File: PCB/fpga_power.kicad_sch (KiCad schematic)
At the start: 11 parts, among them U1 LFE5U-25F-6BG256x

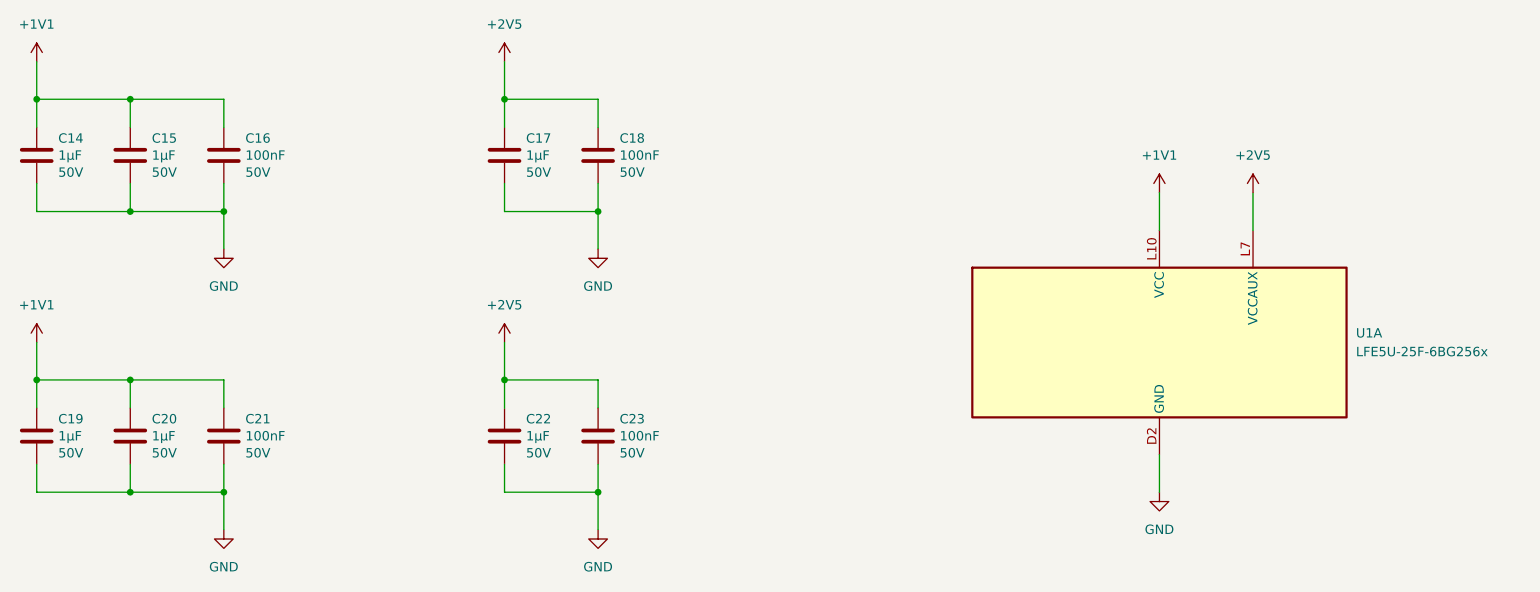
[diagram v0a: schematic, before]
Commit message: Add power supplies
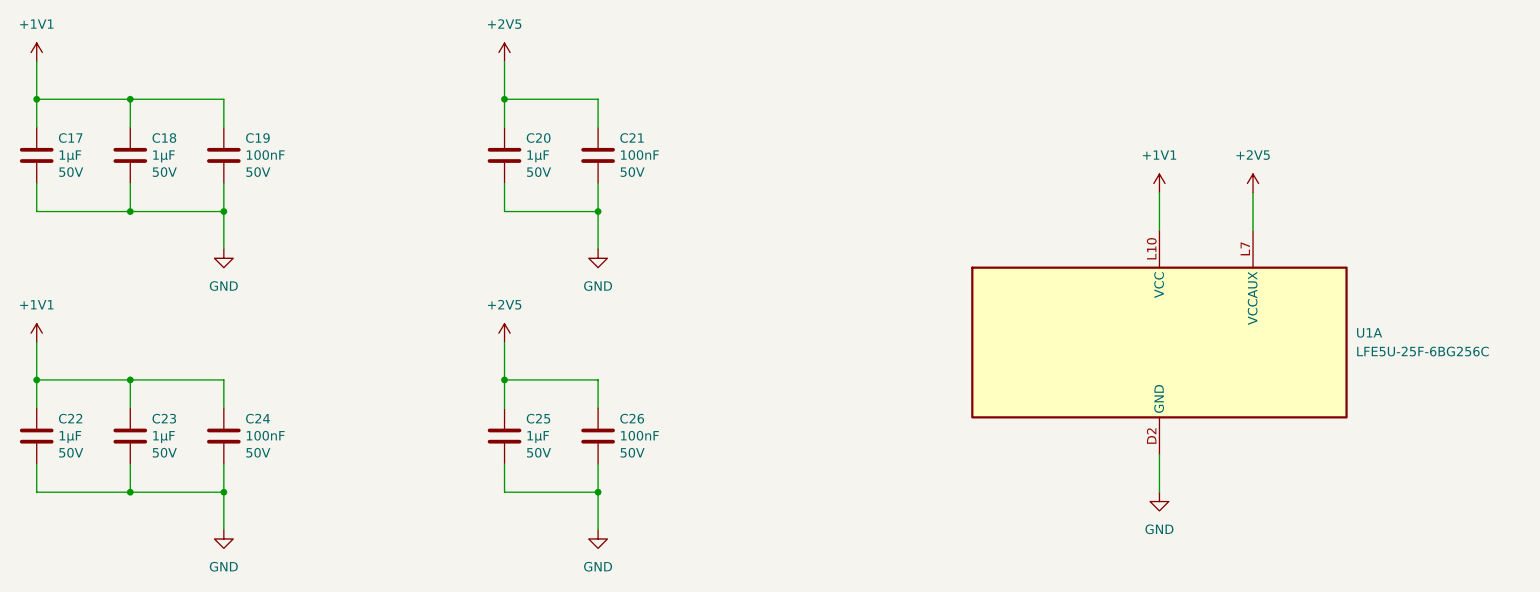
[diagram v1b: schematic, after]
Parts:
- C17: renamed from C14; footprint Capacitor_SMD:C_0603_1608Metric -> Capacitor_SMD:C_0402_1005Metric_Pad0.74x0.62mm_HandSolder; LCSC (none) -> C1518208; Part_number C1608X5R1H105K080AB -> GRM155R61H105KE05D
- C18: renamed from C15; footprint Capacitor_SMD:C_0603_1608Metric -> Capacitor_SMD:C_0402_1005Metric_Pad0.74x0.62mm_HandSolder; LCSC (none) -> C1518208; Part_number C1608X5R1H105K080AB -> GRM155R61H105KE05D
- C19: renamed from C16; footprint Capacitor_SMD:C_0603_1608Metric -> Capacitor_SMD:C_0402_1005Metric_Pad0.74x0.62mm_HandSolder; LCSC (none) -> C77020; Part_number C1608X5R1H104K080AA -> GRM155R71H104KE14D
- C20: renamed from C17; footprint Capacitor_SMD:C_0603_1608Metric -> Capacitor_SMD:C_0402_1005Metric_Pad0.74x0.62mm_HandSolder; LCSC (none) -> C1518208; Part_number C1608X5R1H105K080AB -> GRM155R61H105KE05D
- C21: renamed from C18; footprint Capacitor_SMD:C_0603_1608Metric -> Capacitor_SMD:C_0402_1005Metric_Pad0.74x0.62mm_HandSolder; LCSC (none) -> C77020; Part_number C1608X5R1H104K080AA -> GRM155R71H104KE14D
- C22: renamed from C19; footprint Capacitor_SMD:C_0603_1608Metric -> Capacitor_SMD:C_0402_1005Metric_Pad0.74x0.62mm_HandSolder; LCSC (none) -> C1518208; Part_number C1608X5R1H105K080AB -> GRM155R61H105KE05D
- C23: renamed from C20; footprint Capacitor_SMD:C_0603_1608Metric -> Capacitor_SMD:C_0402_1005Metric_Pad0.74x0.62mm_HandSolder; LCSC (none) -> C1518208; Part_number C1608X5R1H105K080AB -> GRM155R61H105KE05D
- C24: renamed from C21; footprint Capacitor_SMD:C_0603_1608Metric -> Capacitor_SMD:C_0402_1005Metric_Pad0.74x0.62mm_HandSolder; LCSC (none) -> C77020; Part_number C1608X5R1H104K080AA -> GRM155R71H104KE14D
- C25: renamed from C22; footprint Capacitor_SMD:C_0603_1608Metric -> Capacitor_SMD:C_0402_1005Metric_Pad0.74x0.62mm_HandSolder; LCSC (none) -> C1518208; Part_number C1608X5R1H105K080AB -> GRM155R61H105KE05D
- C26: renamed from C23; footprint Capacitor_SMD:C_0603_1608Metric -> Capacitor_SMD:C_0402_1005Metric_Pad0.74x0.62mm_HandSolder; LCSC (none) -> C77020; Part_number C1608X5R1H104K080AA -> GRM155R71H104KE14D
- U1: value LFE5U-25F-6BG256x -> LFE5U-25F-6BG256C; LCSC (none) -> C1521614; Part_number (none) -> LFE5U-25F-6BG256C

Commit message: Add a USB hub
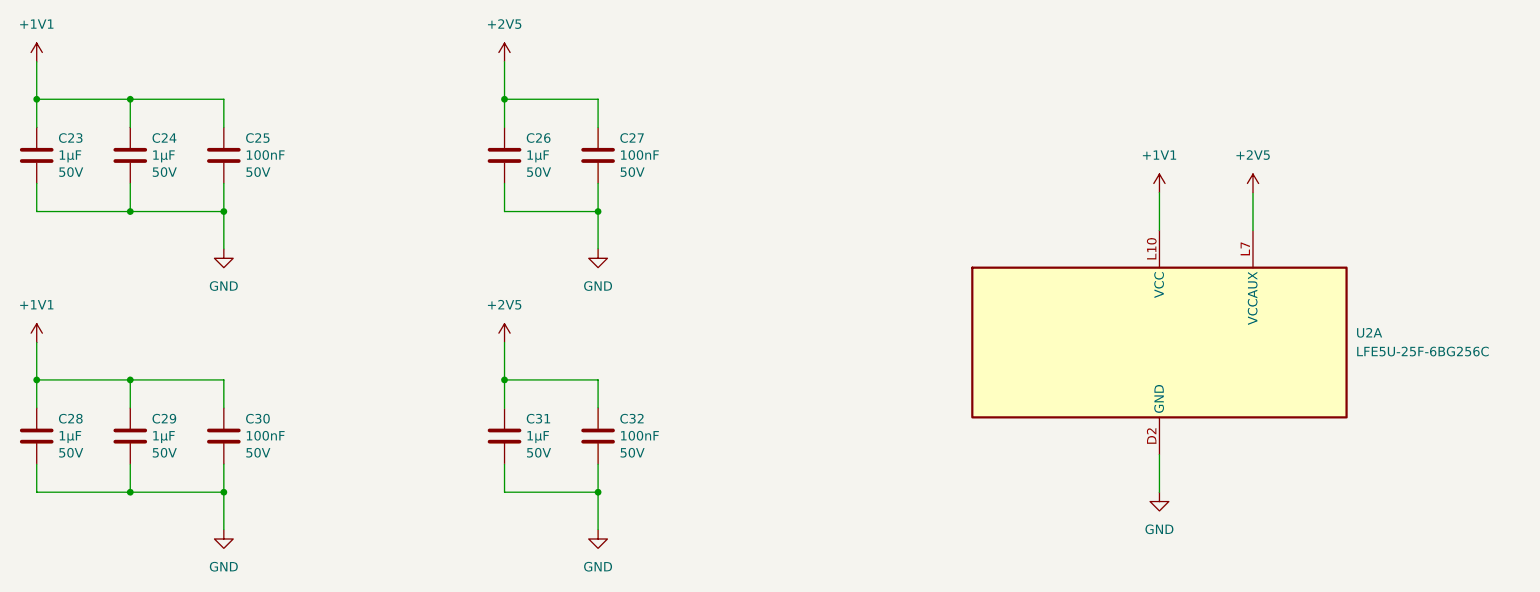
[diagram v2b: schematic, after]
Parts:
- renumbered C17 to C23, C18 to C24, C19 to C25, C20 to C26, C21 to C27, C22 to C28, C23 to C29, C24 to C30, C25 to C31, C26 to C32, U1 to U2
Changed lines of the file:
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@@
 		(on_board yes)
 		(dnp no)
-		(property "Reference" "C17"
+		(property "Reference" "C23"
 			(at 53.721 61.1886 0)
 			(effects
@@
 			(project "clavier"
 				(path "/6362c6e0-59ef-40d3-b6e0-7e9dfe7b9b20/d73938da-f0ba-48e3-aac9-a36988c25c2c/e36c52fe-7af8-49a0-bf3c-a636c30fc9cb"
-					(reference "C17")
+					(reference "C23")
 					(unit 1)
 				)
@@
 		(on_board yes)
 		(dnp no)
-		(property "Reference" "C19"
+		(property "Reference" "C25"
 			(at 79.121 61.1886 0)
 			(effects
@@
 			(project "clavier"
 				(path "/6362c6e0-59ef-40d3-b6e0-7e9dfe7b9b20/d73938da-f0ba-48e3-aac9-a36988c25c2c/e36c52fe-7af8-49a0-bf3c-a636c30fc9cb"
-					(reference "C19")
+					(reference "C25")
 					(unit 1)
 				)
@@
 		(on_board yes)
 		(dnp no)
-		(property "Reference" "C18"
+		(property "Reference" "C24"
 			(at 66.421 61.1886 0)
 			(effects
@@
 			(project "clavier"
 				(path "/6362c6e0-59ef-40d3-b6e0-7e9dfe7b9b20/d73938da-f0ba-48e3-aac9-a36988c25c2c/e36c52fe-7af8-49a0-bf3c-a636c30fc9cb"
-					(reference "C18")
+					(reference "C24")
 					(unit 1)
 				)
@@
 		(on_board yes)
 		(dnp no)
-		(property "Reference" "C23"
+		(property "Reference" "C29"
 			(at 66.421 99.2886 0)
 			(effects
@@
 			(project "clavier"
 				(path "/6362c6e0-59ef-40d3-b6e0-7e9dfe7b9b20/d73938da-f0ba-48e3-aac9-a36988c25c2c/e36c52fe-7af8-49a0-bf3c-a636c30fc9cb"
-					(reference "C23")
+					(reference "C29")
 					(unit 1)
 				)
@@
 		(on_board yes)
 		(dnp no)
-		(property "Reference" "C25"
+		(property "Reference" "C31"
 			(at 117.221 99.2886 0)
 			(effects
@@
 			(project "clavier"
 				(path "/6362c6e0-59ef-40d3-b6e0-7e9dfe7b9b20/d73938da-f0ba-48e3-aac9-a36988c25c2c/e36c52fe-7af8-49a0-bf3c-a636c30fc9cb"
-					(reference "C25")
+					(reference "C31")
 					(unit 1)
 				)
@@
 		(on_board yes)
 		(dnp no)
-		(property "Reference" "C20"
+		(property "Reference" "C26"
 			(at 117.221 61.1886 0)
 			(effects
@@
 			(project "clavier"
 				(path "/6362c6e0-59ef-40d3-b6e0-7e9dfe7b9b20/d73938da-f0ba-48e3-aac9-a36988c25c2c/e36c52fe-7af8-49a0-bf3c-a636c30fc9cb"
-					(reference "C20")
+					(reference "C26")
 					(unit 1)
 				)
@@
 		(dnp no)
 		(fields_autoplaced yes)
-		(property "Reference" "U1"
+		(property "Reference" "U2"
 			(at 229.87 87.6299 0)
 			(effects
@@
 			(project "clavier"
 				(path "/6362c6e0-59ef-40d3-b6e0-7e9dfe7b9b20/d73938da-f0ba-48e3-aac9-a36988c25c2c/e36c52fe-7af8-49a0-bf3c-a636c30fc9cb"
-					(reference "U1")
+					(reference "U2")
 					(unit 1)
 				)
@@
 		(dnp no)
 		(fields_autoplaced yes)
-		(property "Reference" "#PWR030"
+		(property "Reference" "#PWR044"
 			(at 114.3 54.61 0)
 			(effects
@@
 			(project "clavier"
 				(path "/6362c6e0-59ef-40d3-b6e0-7e9dfe7b9b20/d73938da-f0ba-48e3-aac9-a36988c25c2c/e36c52fe-7af8-49a0-bf3c-a636c30fc9cb"
-					(reference "#PWR030")
+					(reference "#PWR044")
 					(unit 1)
 				)
@@
 		(on_board yes)
 		(dnp no)
-		(property "Reference" "C26"
+		(property "Reference" "C32"
 			(at 129.921 99.2886 0)
 			(effects
@@
 			(project "clavier"
 				(path "/6362c6e0-59ef-40d3-b6e0-7e9dfe7b9b20/d73938da-f0ba-48e3-aac9-a36988c25c2c/e36c52fe-7af8-49a0-bf3c-a636c30fc9cb"
-					(reference "C26")
+					(reference "C32")
 					(unit 1)
 				)
@@
 		(dnp no)
 		(fields_autoplaced yes)
-		(property "Reference" "#PWR039"
+		(property "Reference" "#PWR053"
 			(at 127 120.65 0)
 			(effects
@@
 			(project "clavier"
 				(path "/6362c6e0-59ef-40d3-b6e0-7e9dfe7b9b20/d73938da-f0ba-48e3-aac9-a36988c25c2c/e36c52fe-7af8-49a0-bf3c-a636c30fc9cb"
-					(reference "#PWR039")
+					(reference "#PWR053")
 					(unit 1)
 				)
@@
 		(dnp no)
 		(fields_autoplaced yes)
-		(property "Reference" "#PWR032"
+		(property "Reference" "#PWR046"
 			(at 215.9 72.39 0)
 			(effects
@@
 			(project "clavier"
 				(path "/6362c6e0-59ef-40d3-b6e0-7e9dfe7b9b20/d73938da-f0ba-48e3-aac9-a36988c25c2c/e36c52fe-7af8-49a0-bf3c-a636c30fc9cb"
-					(reference "#PWR032")
+					(reference "#PWR046")
 					(unit 1)
 				)
@@
 		(dnp no)
 		(fields_autoplaced yes)
-		(property "Reference" "#PWR031"
+		(property "Reference" "#PWR045"
 			(at 203.2 72.39 0)
 			(effects
@@
 			(project "clavier"
 				(path "/6362c6e0-59ef-40d3-b6e0-7e9dfe7b9b20/d73938da-f0ba-48e3-aac9-a36988c25c2c/e36c52fe-7af8-49a0-bf3c-a636c30fc9cb"
-					(reference "#PWR031")
+					(reference "#PWR045")
 					(unit 1)
 				)
@@
 		(dnp no)
 		(fields_autoplaced yes)
-		(property "Reference" "#PWR034"
+		(property "Reference" "#PWR048"
 			(at 127 82.55 0)
 			(effects
@@
 			(project "clavier"
 				(path "/6362c6e0-59ef-40d3-b6e0-7e9dfe7b9b20/d73938da-f0ba-48e3-aac9-a36988c25c2c/e36c52fe-7af8-49a0-bf3c-a636c30fc9cb"
-					(reference "#PWR034")
+					(reference "#PWR048")
 					(unit 1)
 				)
@@
 		(dnp no)
 		(fields_autoplaced yes)
-		(property "Reference" "#PWR033"
+		(property "Reference" "#PWR047"
 			(at 76.2 82.55 0)
 			(effects
@@
 			(project "clavier"
 				(path "/6362c6e0-59ef-40d3-b6e0-7e9dfe7b9b20/d73938da-f0ba-48e3-aac9-a36988c25c2c/e36c52fe-7af8-49a0-bf3c-a636c30fc9cb"
-					(reference "#PWR033")
+					(reference "#PWR047")
 					(unit 1)
 				)
@@
 		(dnp no)
 		(fields_autoplaced yes)
-		(property "Reference" "#PWR029"
+		(property "Reference" "#PWR043"
 			(at 50.8 54.61 0)
 			(effects
@@
 			(project "clavier"
 				(path "/6362c6e0-59ef-40d3-b6e0-7e9dfe7b9b20/d73938da-f0ba-48e3-aac9-a36988c25c2c/e36c52fe-7af8-49a0-bf3c-a636c30fc9cb"
-					(reference "#PWR029")
+					(reference "#PWR043")
 					(unit 1)
 				)
@@
 		(on_board yes)
 		(dnp no)
-		(property "Reference" "C22"
+		(property "Reference" "C28"
 			(at 53.721 99.2886 0)
 			(effects
@@
 			(project "clavier"
 				(path "/6362c6e0-59ef-40d3-b6e0-7e9dfe7b9b20/d73938da-f0ba-48e3-aac9-a36988c25c2c/e36c52fe-7af8-49a0-bf3c-a636c30fc9cb"
-					(reference "C22")
+					(reference "C28")
 					(unit 1)
 				)
@@
 		(dnp no)
 		(fields_autoplaced yes)
-		(property "Reference" "#PWR037"
+		(property "Reference" "#PWR051"
 			(at 203.2 115.57 0)
 			(effects
@@
 			(project "clavier"
 				(path "/6362c6e0-59ef-40d3-b6e0-7e9dfe7b9b20/d73938da-f0ba-48e3-aac9-a36988c25c2c/e36c52fe-7af8-49a0-bf3c-a636c30fc9cb"
-					(reference "#PWR037")
+					(reference "#PWR051")
 					(unit 1)
 				)
@@
 		(dnp no)
 		(fields_autoplaced yes)
-		(property "Reference" "#PWR035"
+		(property "Reference" "#PWR049"
 			(at 50.8 92.71 0)
 			(effects
@@
 			(project "clavier"
 				(path "/6362c6e0-59ef-40d3-b6e0-7e9dfe7b9b20/d73938da-f0ba-48e3-aac9-a36988c25c2c/e36c52fe-7af8-49a0-bf3c-a636c30fc9cb"
-					(reference "#PWR035")
+					(reference "#PWR049")
 					(unit 1)
 				)
@@
 		(on_board yes)
 		(dnp no)
-		(property "Reference" "C21"
+		(property "Reference" "C27"
 			(at 129.921 61.1886 0)
 			(effects
@@
 			(project "clavier"
 				(path "/6362c6e0-59ef-40d3-b6e0-7e9dfe7b9b20/d73938da-f0ba-48e3-aac9-a36988c25c2c/e36c52fe-7af8-49a0-bf3c-a636c30fc9cb"
-					(reference "C21")
+					(reference "C27")
 					(unit 1)
 				)
@@
 		(dnp no)
 		(fields_autoplaced yes)
-		(property "Reference" "#PWR036"
+		(property "Reference" "#PWR050"
 			(at 114.3 92.71 0)
 			(effects
@@
 			(project "clavier"
 				(path "/6362c6e0-59ef-40d3-b6e0-7e9dfe7b9b20/d73938da-f0ba-48e3-aac9-a36988c25c2c/e36c52fe-7af8-49a0-bf3c-a636c30fc9cb"
-					(reference "#PWR036")
+					(reference "#PWR050")
 					(unit 1)
 				)
@@
 		(dnp no)
 		(fields_autoplaced yes)
-		(property "Reference" "#PWR038"
+		(property "Reference" "#PWR052"
 			(at 76.2 120.65 0)
 			(effects
@@
 			(project "clavier"
 				(path "/6362c6e0-59ef-40d3-b6e0-7e9dfe7b9b20/d73938da-f0ba-48e3-aac9-a36988c25c2c/e36c52fe-7af8-49a0-bf3c-a636c30fc9cb"
-					(reference "#PWR038")
+					(reference "#PWR052")
 					(unit 1)
 				)
@@
 		(on_board yes)
 		(dnp no)
-		(property "Reference" "C24"
+		(property "Reference" "C30"
 			(at 79.121 99.2886 0)
 			(effects
@@
 			(project "clavier"
 				(path "/6362c6e0-59ef-40d3-b6e0-7e9dfe7b9b20/d73938da-f0ba-48e3-aac9-a36988c25c2c/e36c52fe-7af8-49a0-bf3c-a636c30fc9cb"
-					(reference "C24")
+					(reference "C30")
 					(unit 1)
 				)
